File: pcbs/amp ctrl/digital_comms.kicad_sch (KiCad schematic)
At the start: 66 parts, among them J15 RJ45_Shielded, J17 RJ45_Shielded, J88 RJ45_Shielded, Q33 MMBT3904, Q34 MMBT3904, Q35 MMBT3906, Q38 MMBT3904, U21 74LVC2G17, U47 74LVC2G17, U62 FIN1028, U63 FIN1028, U64 FIN1047, U71 FIN1028

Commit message: Backplane comms updates, manufacturing renaming
Removed misspelled "maunfacturing" folder, fixed gitignore rule to remove manufacturing folders within individual PCB folders too
Changed SCKI/SCKO terminology to SCK, SCK_LB (loopback) for clarity
Added ADC_CS loopback signal between amp ctrl board & backplane for better fast-clock timing (#38)
Backplane: changed LVDS FPGA outputs to single-ended FPGA outputs to gain more I/O pins, added external LVDS transceivers (#38)
Backplane: replaced global clock & ~LDAC buffers with a separate FPGA pin for each amp ctrl board (#38)
Backplane: removed +2.5V power supply and level translations, no longer needed without FPGA I/O pins using LVDS_25 I/O configuration
Backplane: replaced +VDC-input resistor with solder jumper (on by default)
Backplane: changed field names (Part Number to MPN) to match Aisler's naming convention for automatic recognition
Amp ctrl: fixed optional level-shifter circuit on each channel for voltage inputs (#9) schematic & channel-1 layout
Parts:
- removed JP71: Jumper_2_Bridged, Jumper:SolderJumper-2_P1.3mm_Bridged_RoundedPad1.0x1.5mm, symbol Jumper:Jumper_2_Bridged
- added JP108: Jumper_2_Bridged, Jumper:SolderJumper-2_P1.3mm_Bridged_RoundedPad1.0x1.5mm, symbol Jumper:Jumper_2_Bridged
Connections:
- net +3V3: no longer U64.2 (DIN1)
- net GND: no longer J15.2
- net ~{ADC_CS}: now also JP108.1 (A)
- net ~{Shutdown}: now also J17.6; no longer J15.1
- net ~{ADC_CS_LB+}: now reaches U64.15 (DOUT1+)
- net ~{ADC_CS_LB+}: now also J15.2
- net ~{ADC_CS_LB-}: now reaches U64.16 (DOUT1-)
- net ~{ADC_CS_LB-}: now also J15.1
- net SCKI renamed SCK
- net SCKI+ renamed SCK+
- net SCKI- renamed SCK-
- net SCKO renamed SCK_LB
- net SCKO+ renamed SCK_LB+
- net SCKO- renamed SCK_LB-
- new net ~{ADC_CS_LB}: JP108.2 (B), U64.2 (DIN1)
- no-connect marks 15 -> 12

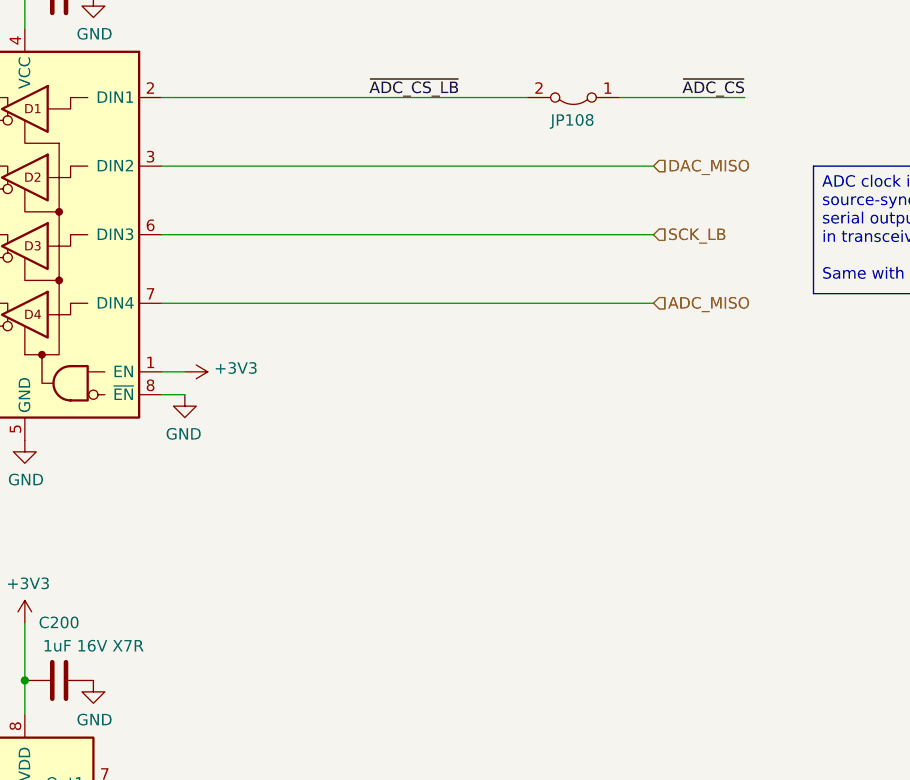
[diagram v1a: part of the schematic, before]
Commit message: Amp ctrl board: added SPI testpoints (fixes #32)
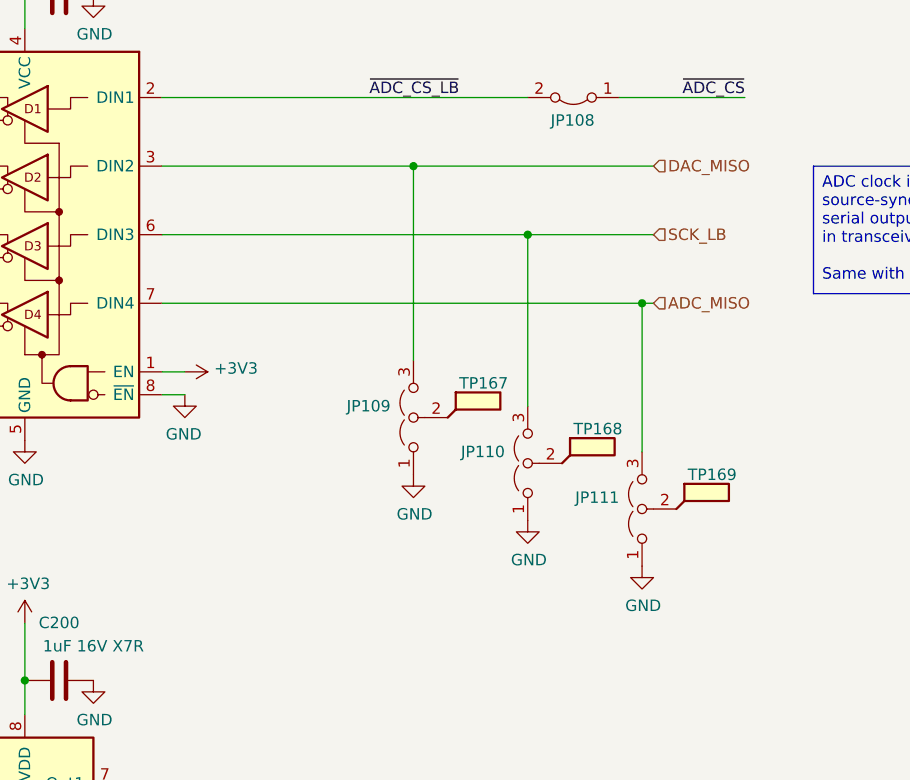
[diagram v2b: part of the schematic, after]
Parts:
- added JP109, JP110, JP111: Jumper_3_Open, Jumper:SolderJumper-3_P2.0mm_Open_TrianglePad1.0x1.5mm, symbol Jumper:Jumper_3_Open
- added TP167, TP168, TP169: TestPoint_Flag, TestPoint:TestPoint_Keystone_5019_Miniature, symbol Connector:TestPoint_Flag
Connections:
- net ADC_MISO: now also JP111.3 (B)
- net DAC_MISO: now also JP109.3 (B)
- net GND: now also JP109.1 (A), JP110.1 (A), JP111.1 (A)
- net SCK_LB: now also JP110.3 (B)
- new net: JP109.2 (C), TP167.1
- new net: JP110.2 (C), TP168.1
- new net: JP111.2 (C), TP169.1
